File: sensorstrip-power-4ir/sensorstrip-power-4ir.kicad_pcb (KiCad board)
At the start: 2 copper layers, 50 x 22 mm, 15 parts, among them J1 USB_C_Receptacle_PowerOnly, J2 Conn_01x02_MountingPin, J3 Conn_01x02_MountingPin, J4 Conn_01x02_MountingPin, J5 Conn_01x02_MountingPin, SW1 SW_DPDT_x2

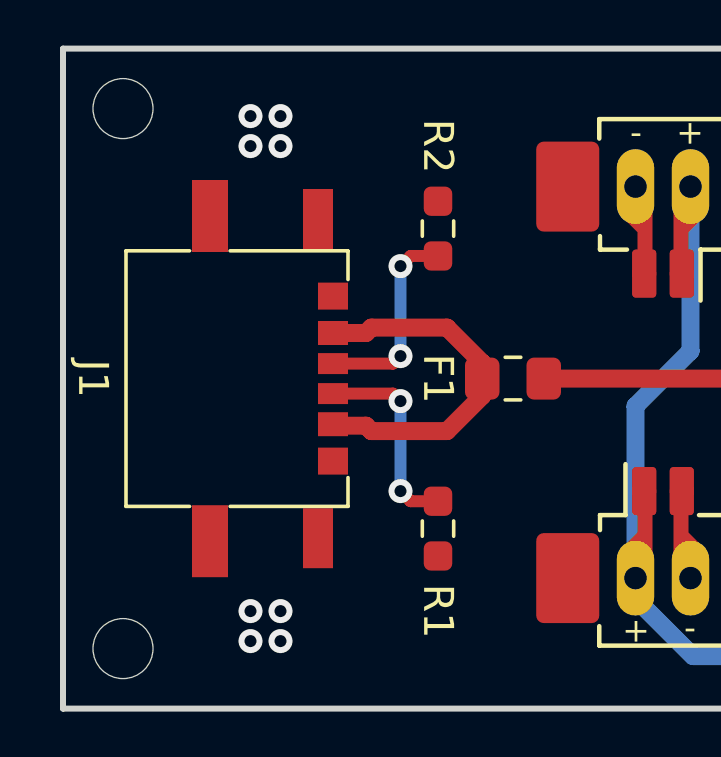
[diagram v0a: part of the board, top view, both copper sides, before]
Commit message: Update USB-C connector
Allowances for GCT USB4135-GF-A footprint
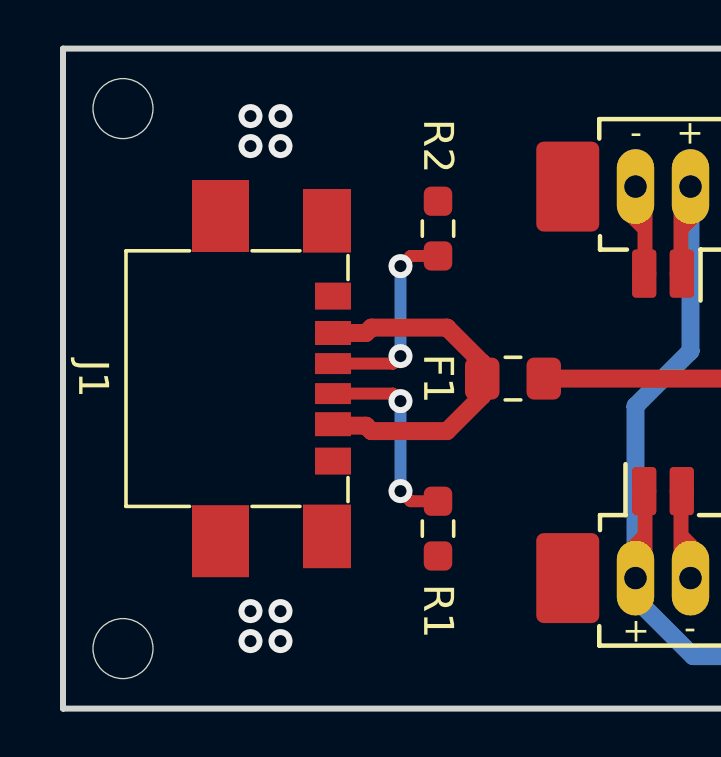
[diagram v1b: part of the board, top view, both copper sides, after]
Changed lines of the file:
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@@
 		)
 		(fp_line
-			(start 4.26 3.43)
-			(end 4.26 -0.5)
+			(start 4.26 2.7)
+			(end 4.26 1.1)
 			(stroke
 				(width 0.12)
@@
 		)
 		(fp_line
-			(start -4.26 -0.5)
-			(end -4.26 3.43)
+			(start -4.26 1.1)
+			(end -4.26 2.7)
 			(stroke
 				(width 0.12)
@@
 		(fp_line
 			(start -3.3 -0.5)
-			(end -4.25 -0.5)
+			(end -4.1 -0.5)
 			(stroke
 				(width 0.12)
@@
 		)
 		(fp_line
-			(start 4.26 -0.5)
+			(start 4.1 -0.5)
 			(end 3.3 -0.5)
 			(stroke
@@
 		(pad "A5" smd rect
 			(at -0.5 0 270)
-			(size 0.7 1)
+			(size 0.7 1.2)
 			(layers "F.Cu" "F.Paste" "F.Mask")
 			(net 2 "/CC1")
@@
 		(pad "A9" smd rect
 			(at 1.52 0 270)
-			(size 0.8 1)
+			(size 0.8 1.2)
 			(layers "F.Cu" "F.Paste" "F.Mask")
 			(net 4 "/VBUS")
@@
 		(pad "A12" smd rect
 			(at 2.75 0 270)
-			(size 0.9 1)
+			(size 0.9 1.2)
 			(layers "F.Cu" "F.Paste" "F.Mask")
 			(net 1 "GND")
@@
 		(pad "B5" smd rect
 			(at 0.5 0 270)
-			(size 0.7 1)
+			(size 0.7 1.2)
 			(layers "F.Cu" "F.Paste" "F.Mask")
 			(net 3 "/CC2")
@@
 		(pad "B9" smd rect
 			(at -1.52 0 270)
-			(size 0.8 1)
+			(size 0.8 1.2)
 			(layers "F.Cu" "F.Paste" "F.Mask")
 			(net 4 "/VBUS")
@@
 		(pad "B12" smd rect
 			(at -2.75 0 270)
-			(size 0.9 1)
+			(size 0.9 1.2)
 			(layers "F.Cu" "F.Paste" "F.Mask")
 			(net 1 "GND")
@@
 		)
 		(pad "S1" smd rect
-			(at -5.42 4.1 270)
-			(size 2.4 1.2)
+			(at -5.42 3.75 270)
+			(size 2.4 1.9)
 			(layers "F.Cu" "F.Paste" "F.Mask")
 			(net 1 "GND")
@@
 		)
 		(pad "S1" smd rect
-			(at -5.32 0.5 270)
-			(size 2 1)
+			(at -5.26 0.2 270)
+			(size 2.12 1.6)
 			(layers "F.Cu" "F.Paste" "F.Mask")
 			(net 1 "GND")
@@
 		)
 		(pad "S1" smd rect
-			(at 5.32 0.5 270)
-			(size 2 1)
+			(at 5.26 0.2 270)
+			(size 2.12 1.6)
 			(layers "F.Cu" "F.Paste" "F.Mask")
 			(net 1 "GND")
@@
 		)
 		(pad "S1" smd rect
-			(at 5.42 4.1 270)
-			(size 2.4 1.2)
+			(at 5.42 3.75 270)
+			(size 2.4 1.9)
 			(layers "F.Cu" "F.Paste" "F.Mask")
 			(net 1 "GND")
